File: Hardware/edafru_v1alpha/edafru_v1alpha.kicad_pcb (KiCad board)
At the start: 2 copper layers, 112 parts, among them J1 ICSP, J3 Conn_01x06_Socket, Q2 MMBT2222A, T1 IRLR2905TRPBF, U1 TLF80511TFV50, U3 PIC18F25K80_ISS, U4 OP07, U5 CJ125, U6 SN65HVD1050D, U7 M95256-WMN6P, Y1 8.000 MHz

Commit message: PCB is developing...
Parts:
- removed the R13 at (67.7, 37.9)
- removed the R14 at (67.7, 40.5)
- removed the R21 at (72.1, 35.4)
- removed the R22 at (72.1, 37.9)
- removed the R44 at (25.1, 27.5)
- removed the R45 at (25.1, 30.0)
- removed the R46 at (25.1, 32.5)
- removed the R47 at (25.1, 35.0)
- removed the R48 at (25.1, 37.5)
- removed the R5 at (63.4, 40.5)
- removed the R6 at (63.4, 43.0)
- added C29: 100nF, Capacitor_SMD:C_0603_1608Metric_Pad1.08x0.95mm_HandSolder, F.Cu at (127.5, 83.6)
- added D5: SZNUP2105L, Package_TO_SOT_SMD:SOT-23, F.Cu at (127.0, 95.2)
- added D6: SZNUP2105L, Package_TO_SOT_SMD:SOT-23, F.Cu at (126.7, 87.5)
- added H1: MountingHole_Pad_MP, MountingHole:MountingHole_3.2mm_M3_ISO14580_Pad, F.Cu at (118.6, 77.9)
- added H2: MountingHole_Pad_MP, MountingHole:MountingHole_3.2mm_M3_ISO14580_Pad, F.Cu at (176.6, 77.9)
- added H3: MountingHole_Pad_MP, MountingHole:MountingHole_3.2mm_M3_ISO14580_Pad, F.Cu at (176.6, 126.9)
- added H4: MountingHole_Pad_MP, MountingHole:MountingHole_3.2mm_M3_ISO14580_Pad, F.Cu at (118.6, 126.9)
- added J1: Raspberry_Pi_4, Connector_PinSocket_2.54mm:PinSocket_2x20_P2.54mm_Vertical, B.Cu at (123.5, 79.2)
- added J2: DE9_Pins_MountingHoles, Connector_Dsub:DSUB-9_Pins_Horizontal_P2.77x2.84mm_EdgePinOffset4.94mm_Housed_MountingHolesOffset4.94mm, F.Cu at (121.3, 97.8)
- added R10: 0R, Resistor_SMD:R_0603_1608Metric_Pad0.98x0.95mm_HandSolder, F.Cu at (172.4, 96.8)
- added R11: 0R, Resistor_SMD:R_0603_1608Metric_Pad0.98x0.95mm_HandSolder, F.Cu at (172.4, 93.8)
- added R15: 0R, Resistor_SMD:R_0603_1608Metric_Pad0.98x0.95mm_HandSolder, F.Cu at (157.3, 90.7)
- added R16: 0R, Resistor_SMD:R_0603_1608Metric_Pad0.98x0.95mm_HandSolder, F.Cu at (157.3, 92.2)
- added R24: 0R, Resistor_SMD:R_0603_1608Metric_Pad0.98x0.95mm_HandSolder, F.Cu at (165.8, 84.6)
- added R25: 0R, Resistor_SMD:R_0603_1608Metric_Pad0.98x0.95mm_HandSolder, F.Cu at (167.3, 84.6)
- added R50: 47K, Resistor_SMD:R_0603_1608Metric_Pad0.98x0.95mm_HandSolder, F.Cu at (143.5, 93.0)
- added R51: 47K, Resistor_SMD:R_0603_1608Metric_Pad0.98x0.95mm_HandSolder, F.Cu at (143.5, 96.0)
- added R52: 47K, Resistor_SMD:R_0603_1608Metric_Pad0.98x0.95mm_HandSolder, F.Cu at (143.5, 94.5)
- added R53: 0R, Resistor_SMD:R_0603_1608Metric_Pad0.98x0.95mm_HandSolder, F.Cu at (130.8, 94.5)
- added R54: 1K, Resistor_SMD:R_0603_1608Metric_Pad0.98x0.95mm_HandSolder, F.Cu at (130.8, 96.0)
- added R55: 47K, Resistor_SMD:R_0603_1608Metric_Pad0.98x0.95mm_HandSolder, F.Cu at (130.8, 91.2)
- added R56: 59R9, Resistor_SMD:R_0603_1608Metric_Pad0.98x0.95mm_HandSolder, F.Cu at (130.8, 85.1)
- added R57: 0R, Resistor_SMD:R_0603_1608Metric_Pad0.98x0.95mm_HandSolder, F.Cu at (130.8, 83.6)
- added R58: 59R9, Resistor_SMD:R_0603_1608Metric_Pad0.98x0.95mm_HandSolder, F.Cu at (130.8, 89.7)
- added R59: 0R, Resistor_SMD:R_0603_1608Metric_Pad0.98x0.95mm_HandSolder, F.Cu at (130.8, 88.1)
- added R60: 0R, Resistor_SMD:R_0603_1608Metric_Pad0.98x0.95mm_HandSolder, F.Cu at (130.8, 86.6)
- added U2: M95256-WMN6P, Package_SO:SOIC-8_3.9x4.9mm_P1.27mm, F.Cu at (151.1, 100.3)
- C18, C19, C20, C21, C22, C23, C24, C25, C4, C6, C7, C9, FB1, FB2, L1, L3: moved to B.Cu
- D4: value SZNUP2105L -> 1N4148W; footprint Package_TO_SOT_SMD:SOT-23 -> Diode_SMD:D_SOD-123
- R23, R7, R8, R9: value 1K -> 0R
- R49: value 0R -> 47K
- TP1: renamed from TP4; moved to B.Cu
- TP2: renamed from TP3; moved to B.Cu
- TP3: renamed from TP5; moved to B.Cu
- TP4: renamed from TP6; moved to B.Cu
- TP5: renamed from TP1; moved to B.Cu
- TP6: renamed from TP2; moved to B.Cu
- TP7: renamed from TP8; moved to B.Cu
- TP8: renamed from TP9; moved to B.Cu
- TP9: renamed from TP7; moved to B.Cu
- U5: footprint ~edafru_v1alpha.kicad_pro:CJ125 -> Package_SO:SOIC-24W_7.5x15.4mm_P1.27mm
- U6: value SN65HVD1050D -> TJA1021T
- U7: value M95256-WMN6P -> SN65HVD1050D; footprint Package_DFN_QFN:WFDFPN-8-1EP_3x2mm_P0.5mm_EP1.25x1.35mm -> Package_SO:SOIC-8_3.9x4.9mm_P1.27mm
- moved C4 191.6 mm to (190.2, 143.2), turned to 180 degrees
- moved C7 191.6 mm to (190.2, 146.5), turned to 180 degrees
- moved TP9 190.0 mm to (204.0, 121.7)
- moved C22 189.5 mm to (196.3, 91.2), turned to 180 degrees
- moved C23 189.5 mm to (196.3, 93.8), turned to 180 degrees
- moved C24 189.5 mm to (196.3, 96.3), turned to 180 degrees
- moved C25 189.5 mm to (196.3, 98.8), turned to 180 degrees
- moved L1 186.8 mm to (190.8, 161.0), turned to 180 degrees
- moved FB1 173.3 mm to (190.4, 152.9), turned to 180 degrees
- moved TP4 170.8 mm to (200.9, 79.2)
- moved R39 170.0 mm to (164.7, 120.4), turned to 180 degrees
- moved TP1 169.2 mm to (198.1, 76.5)
- moved TP8 168.4 mm to (228.6, 82.8)
- moved TP7 168.3 mm to (228.6, 85.1)
- moved R40 166.7 mm to (164.7, 116.6)
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- renumbered J1 to J3, J3 to J4, Q2 to Q1, R10 to R12, R12 to R13, R11 to R14, R15 to R17, R16 to R18, R17 to R19, R18 to R20, R19 to R21, R20 to R22, R24 to R26, R25 to R27, R26 to R28, R27 to R29, R28 to R30, R29 to R31, R30 to R32, R31 to R33, R32 to R34, R33 to R35, R34 to R36, R35 to R37, R36 to R38, R37 to R39, R38 to R40, R39 to R41, R40 to R42, R41 to R43, R42 to R44, R43 to R45, R50 to R46, R52 to R47, R51 to R48, R53 to R5, R54 to R6
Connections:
- net /MCU/ICSP_PGC renamed COM_TX
- net /MCU/ICSP_PGD renamed COM_RX
- C28 pad 1: Net-(C28-Pad1) -> LIN_BUS
- C3 pad 1: Net-(C3-Pad1) -> Net-(D2-K)
- C5 pad 1: +12P -> Net-(D2-K)
- D2 pad 2: +BATT -> Net-(D2-A)
- D4 pad 1: /CAN/CAND_P -> Net-(D4-K)
- D4 pad 2: /CAN/CAND_N -> Net-(D4-A)
- F1 pad 1: Net-(D2-K) -> Net-(D2-A)
- F1 pad 2: Net-(C3-Pad1) -> +BATT
- L2 pad 1: Net-(C3-Pad1) -> Net-(D2-K)
- R23 pad 1: WIDEBAND_SPI1_NSS -> /MCU/EEPROM_W
- R23 pad 2: /MCU/RC2 -> /MCU/RC0
- R49 pad 1: CAN_L -> LIN_D_RX
- R49 pad 2: /CAN/CAND_N -> VCC
- R5 pad 2: Net-(U7-~{HOLD}) -> Net-(U2-~{HOLD})
- R7 pad 1: unconnected-(R7-Pad1) -> /MCU/RA0
- R7 pad 2: /MCU/RA2 -> WIDEBAND_UR
- R8 pad 1: unconnected-(R8-Pad1) -> /MCU/RA1
- R8 pad 2: /MCU/RA3 -> WIDEBAND_UA
- R9 pad 1: /MCU/VSENSE -> /MCU/RA2
- R9 pad 2: /MCU/RA5 -> WIDEBAND_RST
- U6 pad 1: CAN_D_P -> LIN_D_RX
- U6 pad 2: GND -> LIN_SLP_N
- U6 pad 3: VCC -> Net-(U6-~{WAKE})
- U6 pad 4: CAN_D_N -> LIN_D_TX
- U6 pad 5: Net-(U6-VREF) -> GND
- U6 pad 6: /CAN/CAND_N -> Net-(U6-LIN)
- U6 pad 7: /CAN/CAND_P -> +12P
- U6 pad 8: CAN_SLEEP -> Net-(D4-A)
- U7 pad 1: EEPROM_SPI1_NSS -> CAN_D_P
- U7 pad 2: BUS_SP1_MISO -> GND
- U7 pad 3: /MCU/EEPROM_W -> VCC
- U7 pad 4: GND -> CAN_D_N
- U7 pad 5: BUS_SPI1_MOSI -> Net-(U7-VREF)
- U7 pad 6: BUS_SPI1_SCK -> /NETWORK/CAND_N
- U7 pad 7: Net-(U7-~{HOLD}) -> /NETWORK/CAND_P
- U7 pad 8: VCC -> CAN_SLEEP
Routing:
- net (no net): vias 0 -> 4
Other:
- board outline added: 65 x 56.1 mm

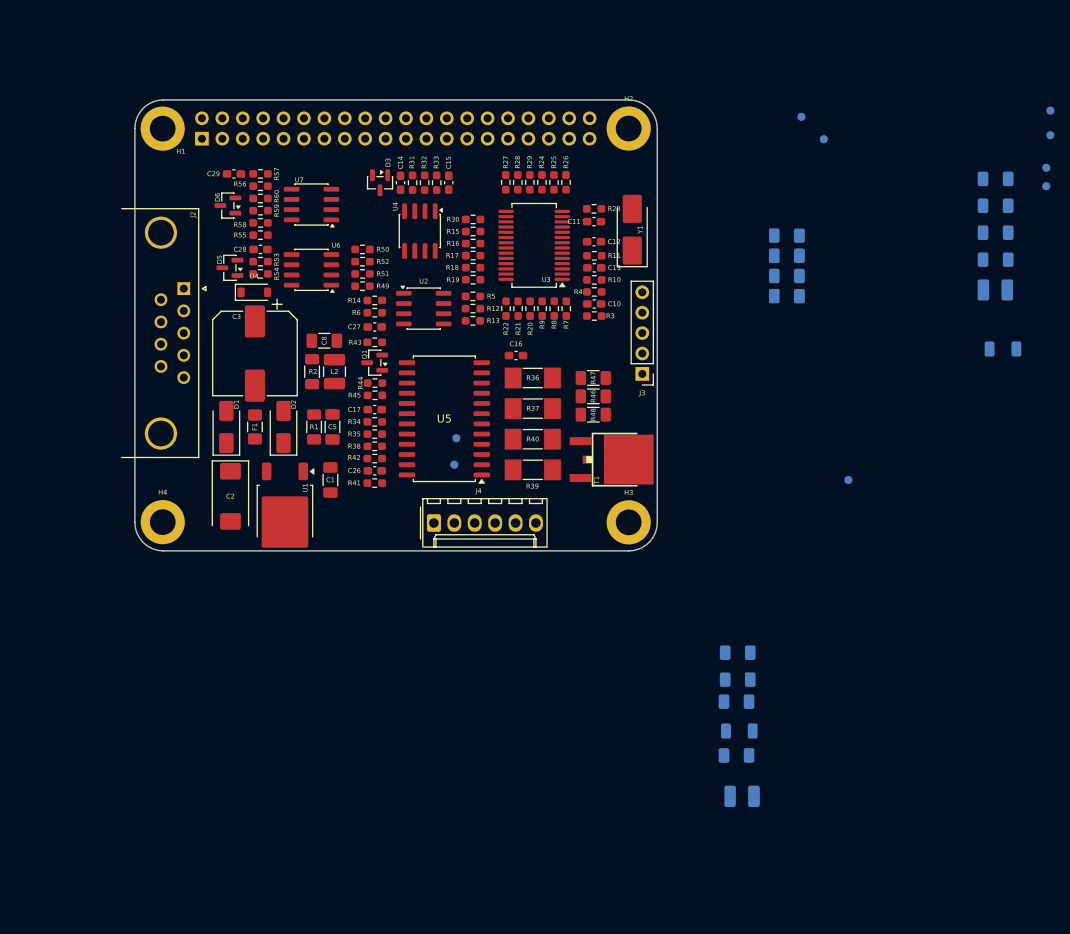
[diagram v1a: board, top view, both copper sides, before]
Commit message: developement is stopped depend on new EDVDU.
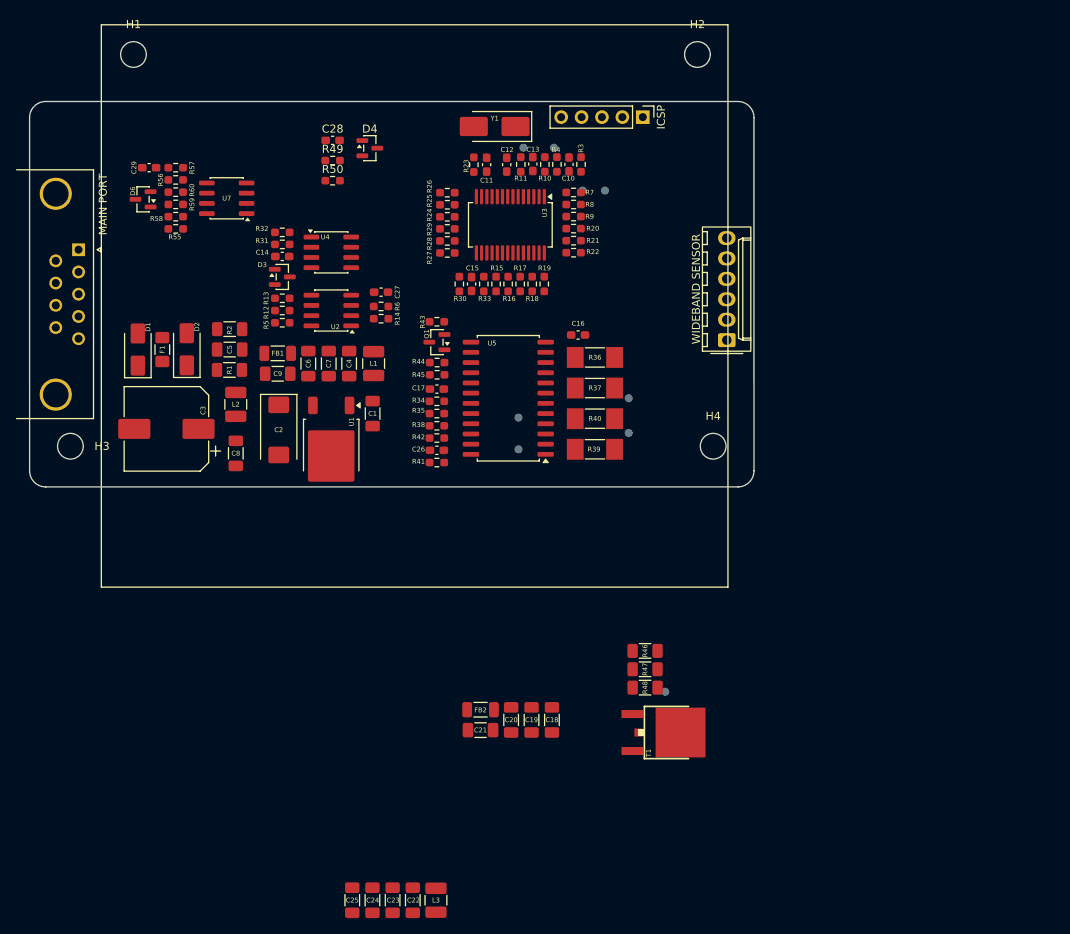
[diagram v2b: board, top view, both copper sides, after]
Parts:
- removed D5: SZNUP2105L, Package_TO_SOT_SMD:SOT-23
- removed J1: Raspberry_Pi_4, Connector_PinSocket_2.54mm:PinSocket_2x20_P2.54mm_Vertical
- removed R51, R52: 47K, Resistor_SMD:R_0603_1608Metric_Pad0.98x0.95mm_HandSolder
- removed R53: 0R, Resistor_SMD:R_0603_1608Metric_Pad0.98x0.95mm_HandSolder
- removed R54: 1K, Resistor_SMD:R_0603_1608Metric_Pad0.98x0.95mm_HandSolder
- removed U6: TJA1021T, Package_SO:SOIC-8_3.9x4.9mm_P1.27mm
- C14: value 10pF -> 100nF
- C18, C19, C20, C21, C22, C23, C24, C25, C4, C6, C7, C9, FB1, FB2, L1, L3: moved to F.Cu
- C5: value 100nF -> 4u7F
- D4: value 1N4148W -> BAT54S; footprint Diode_SMD:D_SOD-123 -> Package_TO_SOT_SMD:SOT-23
- F1: value 3A_Slow_Blow -> 3A Fast Blow
- H1, H2, H3, H4: value MountingHole_Pad_MP -> MountingHole; footprint MountingHole:MountingHole_3.2mm_M3_ISO14580_Pad -> MountingHole:MountingHole_3.2mm_M3_DIN965
- J2: value DE9_Pins_MountingHoles -> MAIN PORT
- J4: value Conn_01x06_Socket -> WIDEBAND SENSOR
- L2: value 47uH -> 2u2H
- R1: value 2R2 -> 1R
- R49: value 47K -> 39K
- R50: value 47K -> 10K
- moved L3 103.0 mm to (152.7, 174.0), turned to -90 degrees
- moved C22 94.9 mm to (149.8, 174.0), turned to -90 degrees
- moved C23 94.0 mm to (147.3, 174.0), turned to -90 degrees
- moved C24 93.3 mm to (144.7, 174.0), turned to -90 degrees
- moved C25 92.6 mm to (142.2, 174.0), turned to -90 degrees
- moved C18 87.1 mm to (167.1, 151.5), turned to -90 degrees
- moved C21 86.8 mm to (158.2, 152.8), turned to 0 degrees
- moved C19 86.2 mm to (164.6, 151.5), turned to -90 degrees
- moved C20 85.5 mm to (162.0, 151.5), turned to -90 degrees
- moved FB2 79.0 mm to (158.2, 150.3), turned to 0 degrees
- moved C9 74.3 mm to (133.0, 108.4), turned to 0 degrees
- moved FB1 74.2 mm to (133.0, 105.9)
- moved L1 70.7 mm to (144.9, 107.2), turned to 90 degrees
- moved H3 70.1 mm to (107.2, 117.5)
- moved H4 69.2 mm to (187.2, 117.5)
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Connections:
- C28 pad 1: LIN_BUS -> IGN_STATUS
- C5 pad 1: Net-(D2-K) -> -BATT
- D4 pad 1: Net-(D4-K) -> GND
- D4 pad 2: Net-(D4-A) -> VCC
- J2 pad 1: unconnected-(J2-Pad1) -> IGN_IN
- J2 pad 4: LIN_INH -> unconnected-(J2-Pad4)
- J2 pad 5: unconnected-(J2-Pad5) -> GNDS
- J2 pad 6: unconnected-(J2-Pad6) -> -BATT
- J2 pad 8: LIN_BUS -> unconnected-(J2-Pad8)
- J2 pad SH: unconnected-(J2-PAD-PadSH) -> GNDS
- R1 pad 2: -BATT -> Net-(D2-K)
- R15 pad 1: /MCU/VSENSE -> IGN_STATUS
- R19 pad 1: CAN_SLEEP -> /MCU/VSENSE
- R20 pad 1: LIN_SLEEP -> CAN_SLEEP
- R29 pad 1: LIN_D_TX -> UART_TX
- R30 pad 1: LIN_D_RX -> UART_RX
- R49 pad 1: LIN_D_RX -> IGN_IN
- R49 pad 2: VCC -> IGN_STATUS
- R50 pad 1: LIN_D_TX -> GND
- R50 pad 2: VCC -> IGN_STATUS
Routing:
- net (no net): vias 4 -> 0
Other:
- board size 65 x 56.1 mm -> 90.2 x 48 mm
